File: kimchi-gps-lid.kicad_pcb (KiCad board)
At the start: 4 copper layers, 65 x 32 mm, 8 parts, among them J1 DF40HC(3.5)-60DS, J2 DF40HC(3.5)-60DS, U1 24C32

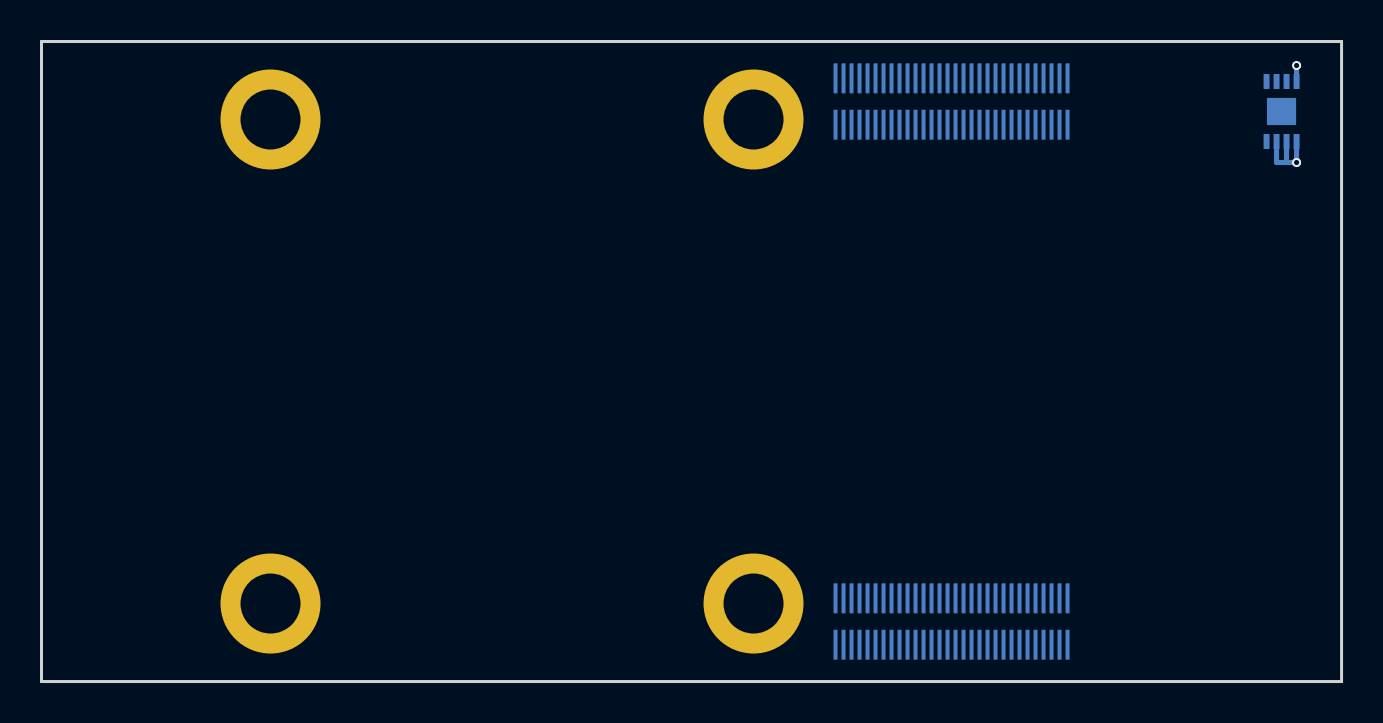
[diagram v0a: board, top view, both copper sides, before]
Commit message: Creating Schematic for the GPS LID
Addition of schematic, datasheets,footprints and 3D Files.

Signed of by: Thore Krug opensource[at]thorekrug.de
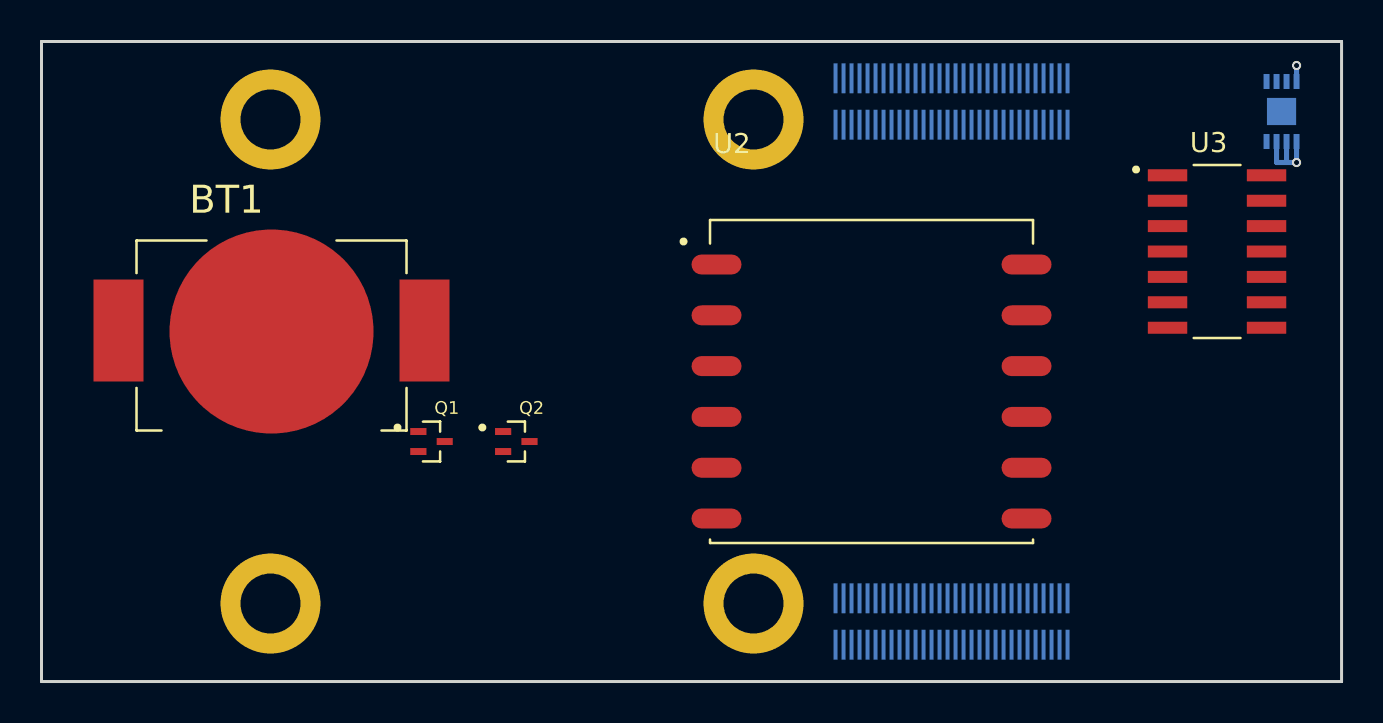
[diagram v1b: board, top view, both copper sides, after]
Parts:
- added BT1: BAT-HLD-012-SMT, gps:BAT_BAT-HLD-012-SMT, F.Cu at (118.5, 108.5)
- added Q1: DTC143ZEBTL, gps:SOTFL50P160X85-3N, F.Cu at (126.5, 114.0)
- added Q2: DTC143ZEBTL, gps:SOTFL50P160X85-3N, F.Cu at (130.7, 114.0)
- added U2: L80RE-M37, gps:XCVR_L80RE-M37, F.Cu at (148.5, 111.5)
- added U3: TXS0104ED, gps:SOIC127P600X175-14N, F.Cu at (165.8, 104.5)
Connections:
- J1 pad 1: (no net) -> /USDHC3_CMD
- J1 pad 17: (no net) -> I2C3_SDA
- J1 pad 18: (no net) -> I2C3_SCL
- J1 pad 19: (no net) -> I2C2_SDA
- J1 pad 2: (no net) -> /USDHC3_CLK
- J1 pad 20: (no net) -> I2C2_SCL
- J1 pad 21: (no net) -> I2C1_SDA
- J1 pad 22: (no net) -> I2C1_SCL
- J1 pad 23: (no net) -> ECSPI1_SCLK
- J1 pad 24: (no net) -> ECSPI1_SS0
- J1 pad 25: (no net) -> ECSPI1_MOSI
- J1 pad 26: (no net) -> ECSPI1_MISO
- J1 pad 27: (no net) -> ECSPI2_SCLK
- J1 pad 28: (no net) -> ECSPI2_SS0
- J1 pad 29: (no net) -> ECSPI2_MOSI
- J1 pad 3: (no net) -> /USDHC3_DATA3
- J1 pad 30: (no net) -> ECSPI2_MISO
- J1 pad 31: (no net) -> /DISP_D0_N
- J1 pad 32: (no net) -> /DISP_D0_P
- J1 pad 33: (no net) -> /DISP_D1_N
- J1 pad 34: (no net) -> /DISP_D1_P
- J1 pad 35: (no net) -> /DISP_CK_N
- J1 pad 36: (no net) -> /DISP_CK_P
- J1 pad 37: (no net) -> /DISP_D2_N
- J1 pad 38: (no net) -> /DISP_D2_P
- J1 pad 39: (no net) -> /DISP_D3_N
- J1 pad 4: (no net) -> /USDHC3_DATA0
- J1 pad 40: (no net) -> /DISP_D3_P
- J1 pad 41: (no net) -> /CAM_D0_N
- J1 pad 42: (no net) -> /CAM_D0_P
- J1 pad 43: (no net) -> /CAM_D1_N
- J1 pad 44: (no net) -> /CAM_D1_P
- J1 pad 45: (no net) -> /CAM_CK_N
- J1 pad 46: (no net) -> /CAM_CK_P
- J1 pad 47: (no net) -> /CAM_D2_N
- J1 pad 48: (no net) -> /CAM_D2_P
- J1 pad 49: (no net) -> /CAM_D3_N
- J1 pad 5: (no net) -> /USDHC3_DATA1
- J1 pad 50: (no net) -> /CAM_D3_P
- J1 pad 52: (no net) -> UIM_VPP
- J1 pad 53: (no net) -> UIM_RESET_N
- J1 pad 54: (no net) -> UIM_CLK
- J1 pad 55: (no net) -> UIM_DATA
- J1 pad 56: (no net) -> UIM_PWR
- J1 pad 57: (no net) -> USB2_VBUS
- J1 pad 58: (no net) -> USB2_ID
- J1 pad 59: (no net) -> USB2_DN
- J1 pad 6: (no net) -> /USDHC3_DATA2
- J1 pad 60: (no net) -> USB2_DP
- J2 pad 1: (no net) -> /ENET_MDIO
- J2 pad 10: (no net) -> /ENET_TD0
- J2 pad 11: (no net) -> /ENET_TD3
- J2 pad 12: (no net) -> /ENET_TD2
- J2 pad 13: (no net) -> /ENET_TX_CTL
- J2 pad 14: (no net) -> /ENET_TXC
- J2 pad 15: (no net) -> SAI2_RXD0
- J2 pad 16: (no net) -> SAI2_TXFS
- J2 pad 17: (no net) -> SAI2_RXC
- J2 pad 18: (no net) -> SAI2_TXD0
- J2 pad 19: (no net) -> SAI2_TXC
- J2 pad 2: (no net) -> /ENET_MDC
- J2 pad 20: (no net) -> SAI2_MCLK
- J2 pad 21: (no net) -> SAI2_RXFS
- J2 pad 22: (no net) -> GPIO1[15]
- J2 pad 23: (no net) -> GPIO1[14]
- J2 pad 24: (no net) -> GPIO1[13]
- J2 pad 25: (no net) -> GPIO1[12]
- J2 pad 26: (no net) -> GPIO1[11]
- J2 pad 27: (no net) -> GPIO1[10]
- J2 pad 28: (no net) -> GPIO1[9]
- J2 pad 29: (no net) -> GPIO1[1]
- J2 pad 3: (no net) -> /ENET_RD3
- J2 pad 30: (no net) -> GPIO1[0]
- J2 pad 31: (no net) -> SAI3_TXC
- J2 pad 32: (no net) -> SAI3_TXD
- J2 pad 33: (no net) -> SAI3_RXD
- J2 pad 34: (no net) -> SAI3_RXFS
- J2 pad 35: (no net) -> SAI3_RXC
- J2 pad 36: (no net) -> SAI3_TXFS
- J2 pad 37: (no net) -> SAI3_MCLK
- J2 pad 4: (no net) -> /ENET_RD1
- J2 pad 46: (no net) -> UART1_TX
- J2 pad 47: (no net) -> UART1_RX
- J2 pad 48: (no net) -> UART3_TX
- J2 pad 49: (no net) -> UART3_RX
- J2 pad 5: (no net) -> /ENET_RD2
- J2 pad 58: (no net) -> Net-(J2-Pad58)
- J2 pad 59: (no net) -> PCIE_USB_D_P
- J2 pad 6: (no net) -> /ENET_RD0
- J2 pad 60: (no net) -> PCIE_USB_D_N
- J2 pad 7: (no net) -> /ENET_RXC
- J2 pad 8: (no net) -> /ENET_RX_CTL
- J2 pad 9: (no net) -> /ENET_TD1

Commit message: Completed routing, minor fixes remaining
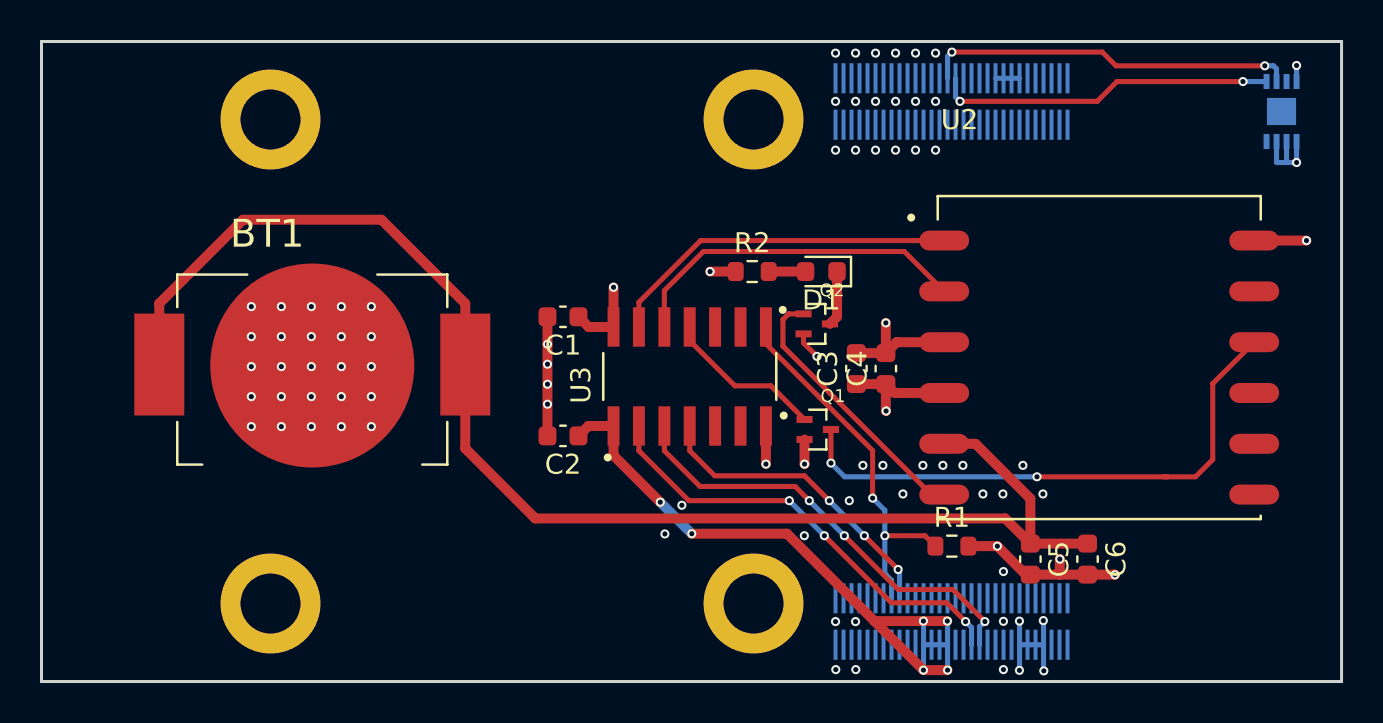
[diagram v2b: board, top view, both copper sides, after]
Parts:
- added C1: 100n, Capacitor_SMD:C_0603_1608Metric, F.Cu at (133.1, 107.8)
- added C2: 100n, Capacitor_SMD:C_0603_1608Metric, F.Cu at (133.1, 113.7)
- added C3: 10uF, Capacitor_SMD:C_0603_1608Metric, F.Cu at (147.7, 110.4)
- added C4: 100n, Capacitor_SMD:C_0603_1608Metric, F.Cu at (149.2, 110.4)
- added C5: 4,7uF, Capacitor_SMD:C_0603_1608Metric, F.Cu at (156.4, 119.9)
- added C6: 100n, Capacitor_SMD:C_0603_1608Metric, F.Cu at (159.3, 119.9)
- added D1: LED, LED_SMD:LED_0603_1608Metric, F.Cu at (146.0, 105.5)
- added R1: 10K, Resistor_SMD:R_0603_1608Metric, F.Cu at (152.5, 119.2)
- added R2: R, Resistor_SMD:R_0603_1608Metric, F.Cu at (142.5, 105.5)
- moved U3 27.1 mm to (139.4, 110.7), turned to 90 degrees
- moved Q1 19.3 mm to (145.8, 113.4)
- moved Q2 16.1 mm to (145.8, 108.1)
- moved U2 11.4 mm to (159.9, 110.3)
- moved BT1 2.65 mm to (120.5, 110.2)
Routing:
- net V_BCKP: track 0.00 -> 69.8 mm
- net VDD_1V8: track 0.00 -> 34.4 mm, vias 0 -> 6
- net RESET: track 0.00 -> 28.4 mm, vias 0 -> 2
- net GND: track 0.00 -> 27.9 mm, vias 0 -> 76
- net UART3_TX: track 0.00 -> 22.4 mm, vias 0 -> 3
- net UART3_RX: track 0.00 -> 22.1 mm, vias 0 -> 3
- net GPIO1[14]: track 0.00 -> 19.7 mm, vias 0 -> 2
- net I2C4_SCL: track 0.00 -> 18.6 mm, vias 0 -> 2
- net /RXD1: track 0.00 -> 17.8 mm
- net /TXD1: track 0.00 -> 17.4 mm
- net VDD_3V3: track 4.95 -> 22.3 mm, vias 2 -> 9
- net I2C4_SDA: track 0.00 -> 17.0 mm, vias 0 -> 2
- net GPIO1[15]: track 0.00 -> 15.6 mm, vias 0 -> 3
- net 1PPS: track 0.00 -> 13.6 mm
- net RESET-GPIO: track 0.00 -> 8.06 mm
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
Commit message: Updated routing to reduce vias and cross-overs
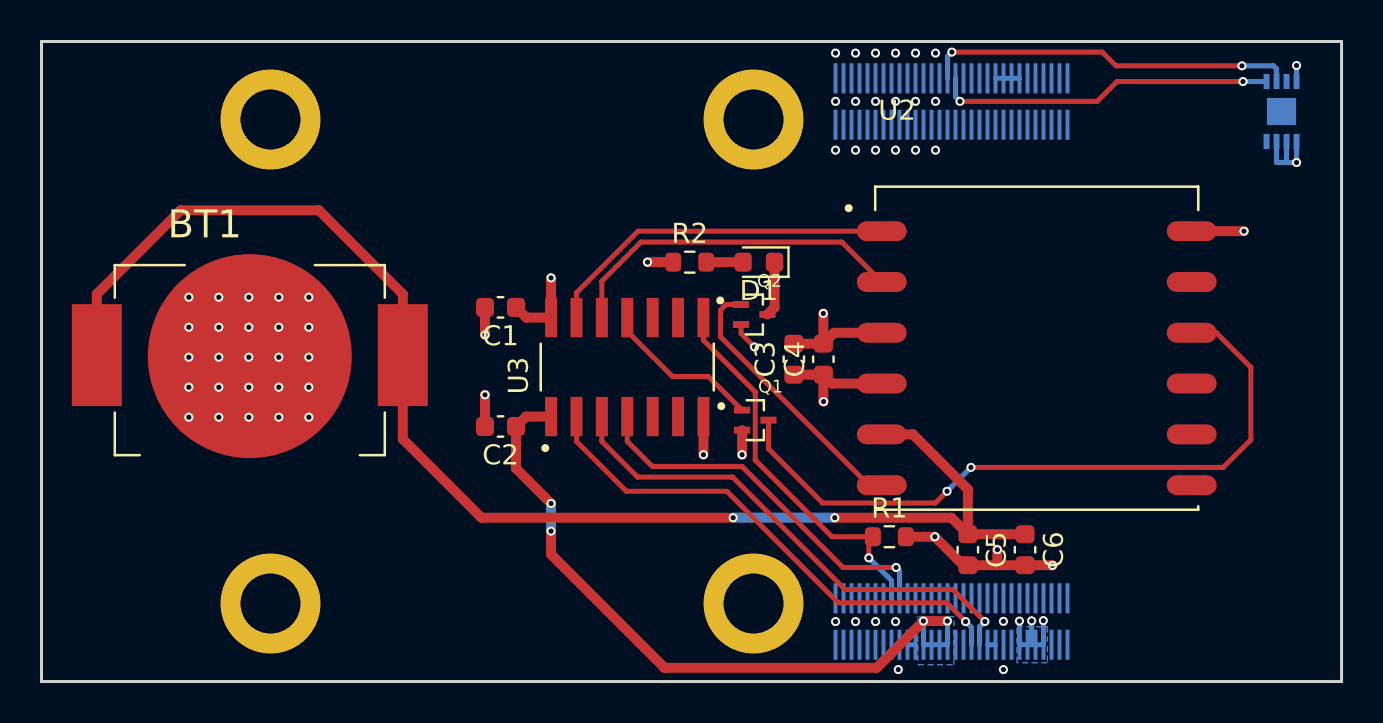
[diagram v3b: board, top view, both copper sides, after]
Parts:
- moved C4 3.16 mm to (146.1, 109.9)
- moved C5 3.16 mm to (153.3, 119.4)
- moved R1 3.16 mm to (149.4, 118.8)
- moved U2 3.16 mm to (156.8, 109.8)
- moved U3 3.16 mm to (136.3, 110.3)
- moved BT1 3.16 mm to (117.4, 109.7)
- moved C1 3.16 mm to (129.9, 107.3)
- moved C2 3.16 mm to (129.9, 113.2)
- moved C3 3.16 mm to (144.6, 109.9)
- moved C6 3.16 mm to (156.2, 119.4)
- moved D1 3.16 mm to (142.9, 105.0)
- moved Q1 3.16 mm to (142.7, 112.9)
- moved Q2 3.16 mm to (142.6, 107.6)
- moved R2 3.16 mm to (139.4, 105.0)
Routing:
- net RESET: track 28.4 -> 35.3 mm
- net GPIO1[15]: track 15.6 -> 18.9 mm, vias 3 -> 1
- net UART3_RX: track 22.1 -> 25.4 mm, vias 3 -> 1
- net UART3_TX: track 22.4 -> 25.7 mm, vias 3 -> 1
- net GND: track 27.9 -> 25.7 mm, vias 76 -> 60
- net VDD_1V8: track 34.4 -> 35.8 mm, vias 6 -> 4
- net VDD_3V3: track 22.3 -> 21.0 mm, vias 9 -> 8
- net GPIO1[14]: vias 2 -> 1
- net V_BCKP: vias 0 -> 2
- added copper zone on B.Cu, net VDD_1V8
- added copper zone on B.Cu, net VDD_3V3
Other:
- rule trace_min: 0.0762 -> 0.2
- rule via_min_size: 0.3048 -> 0.4

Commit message: Minor change in VDD_1v8 routing
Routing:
- net VDD_1V8: track 35.8 -> 36.7 mm
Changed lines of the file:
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@@
     (thickness 1.6)
     (drawings 42)
-    (tracks 252)
+    (tracks 253)
     (zones 0)
     (modules 22)
@@
   )
   (setup
-    (last_trace_width 0.254)
+    (last_trace_width 0.5)
     (user_trace_width 0.0762)
     (user_trace_width 0.0889)
@@
   (via (at 151.0944 122.9774) (size 0.4572) (drill 0.254) (layers F.Cu B.Cu) (net 3))
   (segment (start 152.2882 122.9774) (end 151.0944 122.9774) (width 0.5) (layer F.Cu) (net 3))
-  (via (at 132.4762 118.4816) (size 0.4572) (drill 0.254) (layers F.Cu B.Cu) (net 3))
+  (segment (start 130.7239 113.2492) (end 130.7239 115.345) (width 0.5) (layer F.Cu) (net 3))
+  (via (at 130.7236 117.0338) (size 0.4572) (drill 0.254) (layers F.Cu B.Cu) (net 3))
+  (segment (start 130.7239 117.0335) (end 130.7236 117.0338) (width 0.5) (layer F.Cu) (net 3))
+  (segment (start 130.7239 115.345) (end 130.7239 117.0335) (width 0.5) (layer F.Cu) (net 3))
+  (via (at 130.7236 118.5197) (size 0.4572) (drill 0.254) (layers F.Cu B.Cu) (net 3))
+  (segment (start 130.7236 117.0338) (end 130.7236 118.5197) (width 0.5) (layer B.Cu) (net 3))
   (segment (start 148.7576 125.3142) (end 151.0944 122.9774) (width 0.5) (layer F.Cu) (net 3))
-  (segment (start 138.1531 125.3142) (end 148.7576 125.3142) (width 0.5) (layer F.Cu) (net 3))
-  (segment (start 132.4762 119.6373) (end 138.1531 125.3142) (width 0.5) (layer F.Cu) (net 3))
-  (segment (start 132.4762 118.4816) (end 132.4762 119.6373) (width 0.5) (layer F.Cu) (net 3))
-  (segment (start 132.4762 118.4816) (end 132.4762 117.0973) (width 0.5) (layer B.Cu) (net 3))
-  (via (at 132.4762 117.0973) (size 0.4572) (drill 0.254) (layers F.Cu B.Cu) (net 3))
-  (segment (start 130.7239 115.345) (end 132.4762 117.0973) (width 0.5) (layer F.Cu) (net 3))
-  (segment (start 130.7239 113.2492) (end 130.7239 115.345) (width 0.5) (layer F.Cu) (net 3))
+  (segment (start 136.5021 125.3142) (end 148.7576 125.3142) (width 0.5) (layer F.Cu) (net 3))
+  (segment (start 130.7236 119.5357) (end 136.5021 125.3142) (width 0.5) (layer F.Cu) (net 3))
+  (segment (start 130.7236 118.5197) (end 130.7236 119.5357) (width 0.5) (layer F.Cu) (net 3))
   (via (at 169.75 95.2) (size 0.4572) (drill 0.254) (layers F.Cu B.Cu) (net 4))
   (segment (start 169.75 96) (end 169.75 95.2) (width 0.254) (layer B.Cu) (net 4))

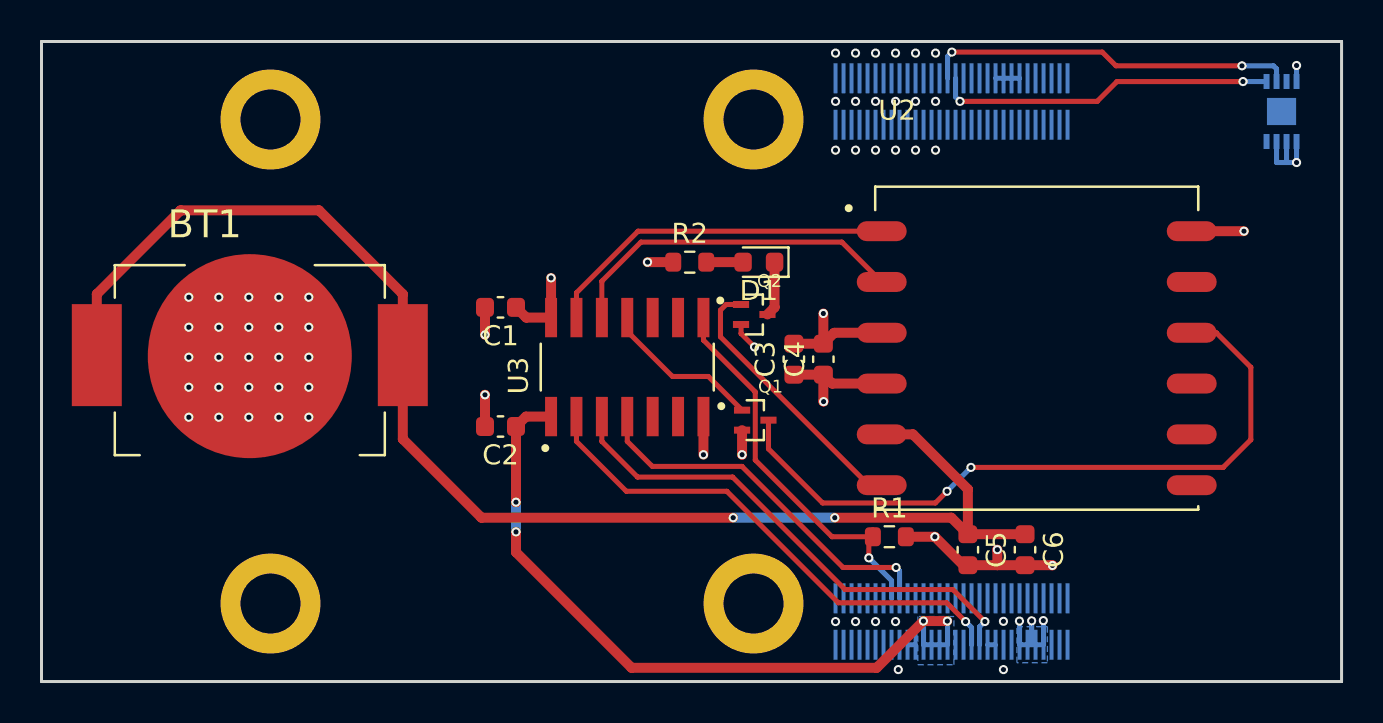
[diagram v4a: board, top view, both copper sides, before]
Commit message: Fixed silkscreen and added square keepout under gps module
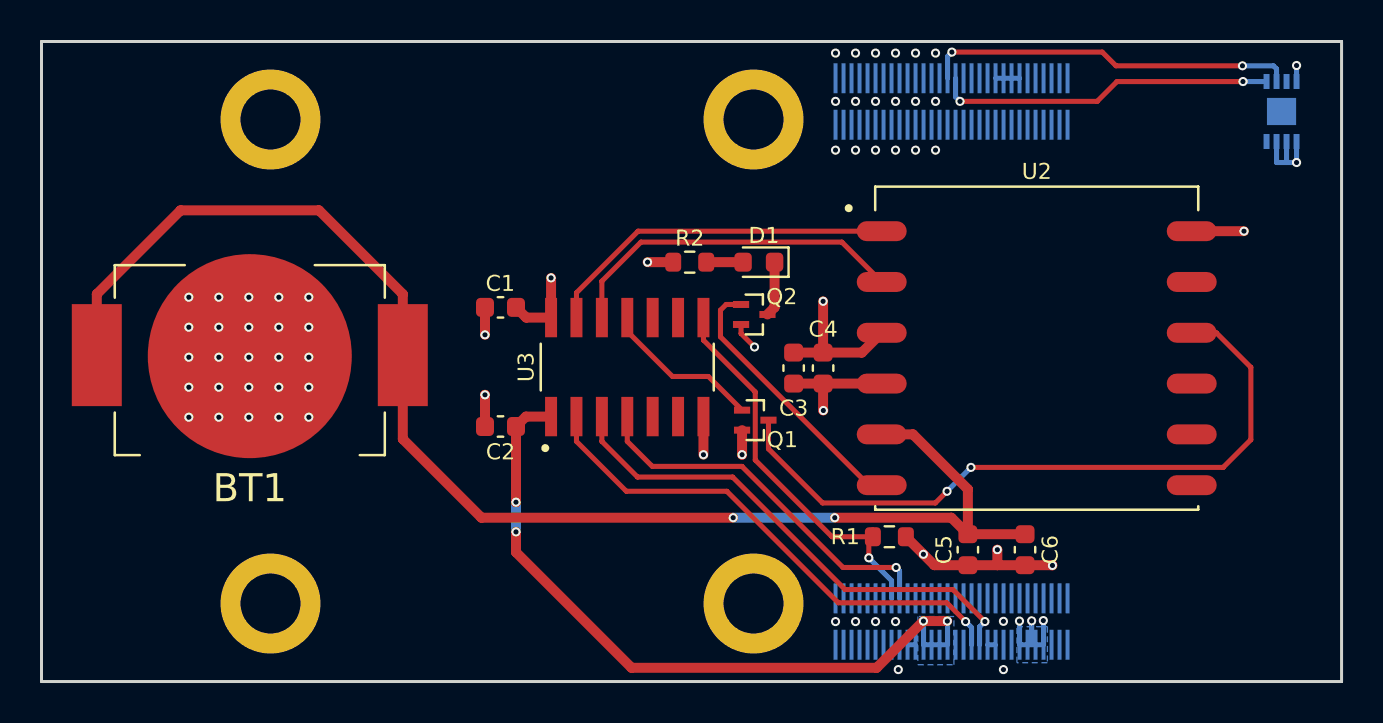
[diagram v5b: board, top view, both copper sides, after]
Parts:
- moved C3 0.44 mm to (144.6, 110.3)
- moved C4 0.44 mm to (146.1, 110.3)
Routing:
- net GND: track 25.7 -> 27.0 mm

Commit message: Update layout and routing
Signed-off-by: Michael Welling <mwelling@ieee.org>
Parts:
- moved R2 27.0 mm to (159.3, 123.2)
- moved D1 23.3 mm to (159.3, 121.5), turned to 0 degrees
- moved Q2 19.5 mm to (156.4, 121.5)
- moved R1 14.0 mm to (143.1, 106.2)
- moved C6 13.2 mm to (143.9, 114.5)
- moved Q1 12.8 mm to (134.2, 103.3), turned to 90 degrees
- moved C5 11.9 mm to (142.4, 114.5)
- moved BT1 3.43 mm to (114.0, 110.2), turned to 270 degrees
- moved C3 2.20 mm to (142.4, 110.3)
- moved C4 2.20 mm to (143.9, 110.3)
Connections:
- U3 pad 11: RESET-GPIO -> /TXD1
- U3 pad 12: /TXD1 -> /RXD1
- U3 pad 13: /RXD1 -> RESET-GPIO
- U3 pad 2: UART3_TX -> GPIO1[15]
- U3 pad 3: UART3_RX -> UART3_TX
- U3 pad 4: GPIO1[15] -> UART3_RX
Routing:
- net V_BCKP: track 69.8 -> 58.9 mm, vias 2 -> 0
- net GND: track 27.0 -> 17.6 mm, vias 60 -> 59
- net RESET: track 35.3 -> 42.8 mm, vias 2 -> 0
- net GPIO1[15]: track 18.9 -> 23.5 mm
- net RESET-GPIO: track 8.06 -> 3.86 mm
- net 1PPS: track 13.6 -> 9.45 mm
- net VDD_1V8: track 36.7 -> 33.8 mm, vias 4 -> 2
- net GPIO1[14]: track 19.7 -> 22.2 mm
- net /TXD1: track 17.4 -> 15.2 mm
- net Net-(D1-Pad1): track 2.76 -> 1.50 mm
- net VDD_3V3: track 20.8 -> 21.8 mm, vias 8 -> 7
- net UART3_TX: track 25.7 -> 26.7 mm
- net UART3_RX: track 25.4 -> 26.1 mm
- added copper zone on F.Cu, net GND
